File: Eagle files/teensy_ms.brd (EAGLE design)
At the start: 36 x 50 mm, 14 parts, among them IC1 SN65HVD230, IC2 TEENSY_3.0_BASIC-MIN

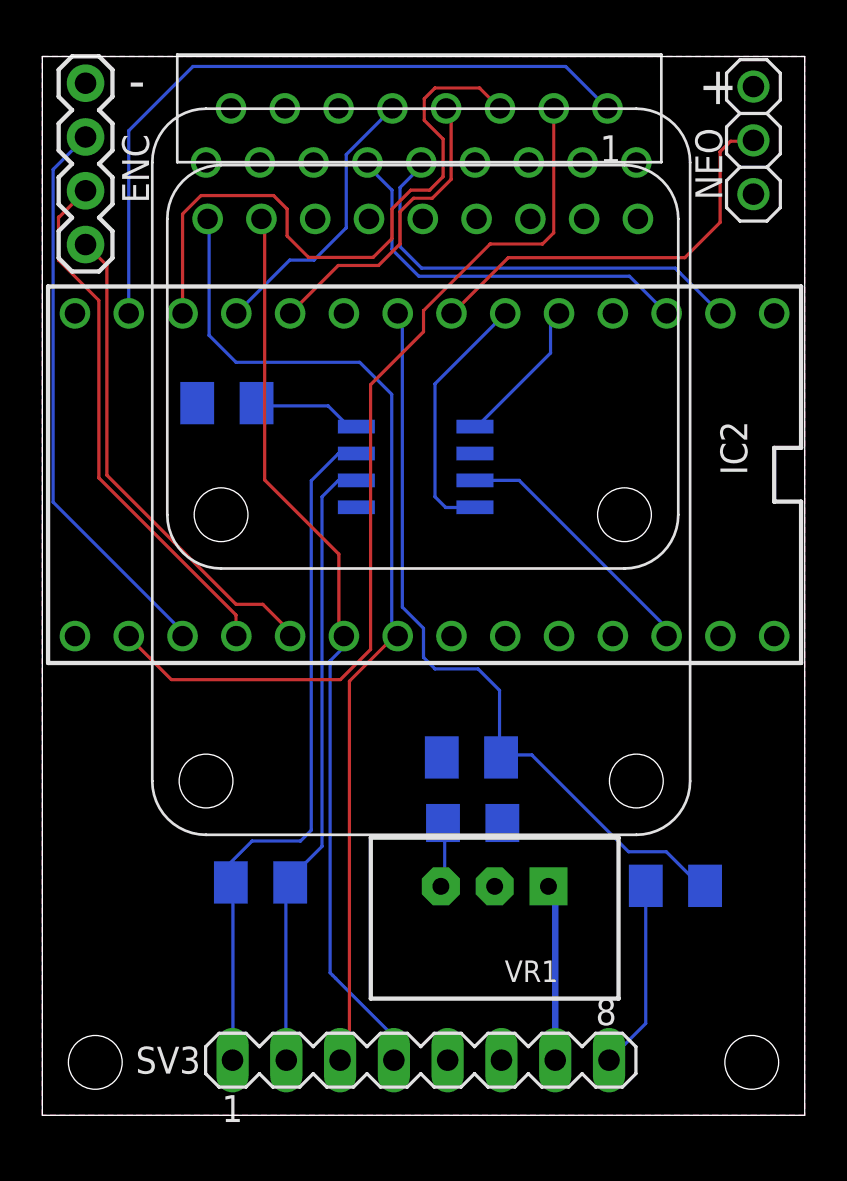
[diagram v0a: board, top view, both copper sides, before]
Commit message: Remove GPS and Accel from PCB
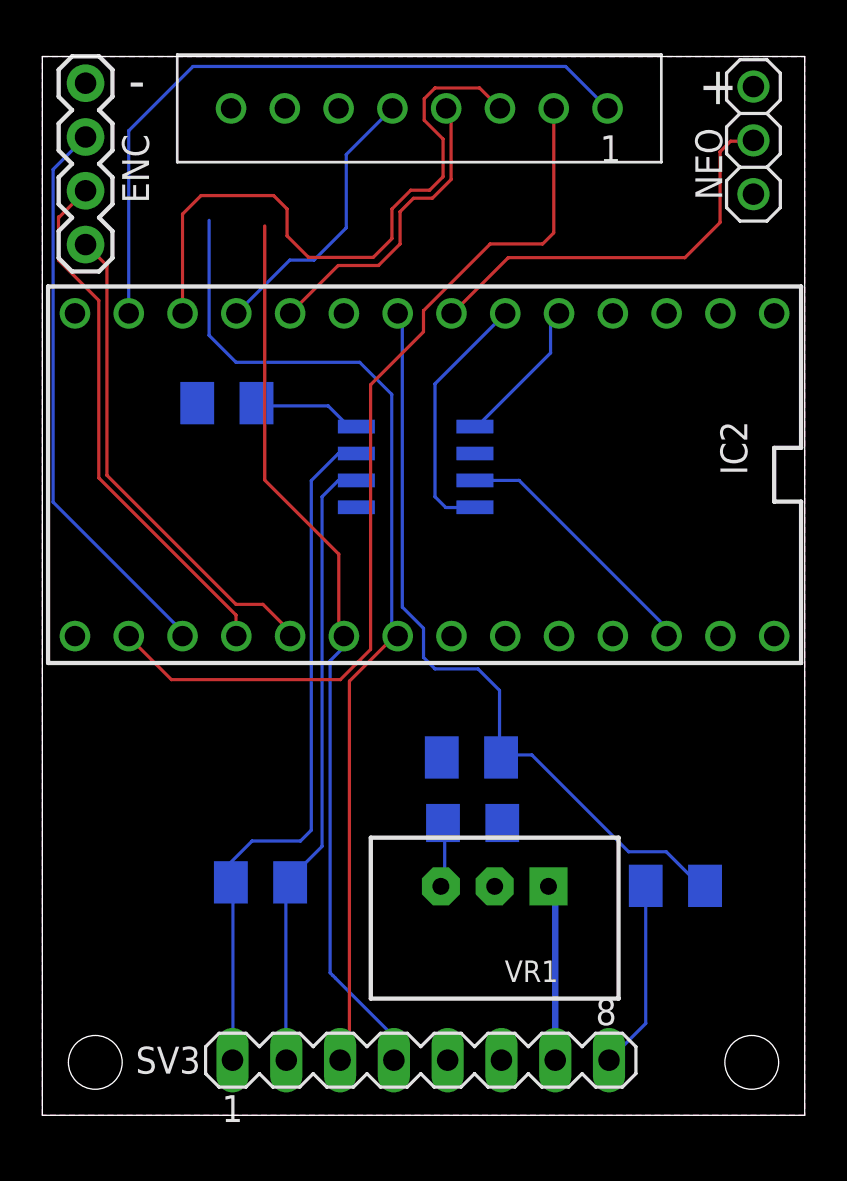
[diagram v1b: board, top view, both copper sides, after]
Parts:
- removed U$3: ACCELEROMETER, custom:ACCELEROMETER
- removed U$5: ULTIMATEGPS, custom:ULTIMATEGPS
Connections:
- removed net N$4: IC2.1, U$5.4
- removed net N$5: IC2.0, U$5.5
- net GND: no longer U$3.7, U$5.3
- net N$14: no longer U$3.1
- net N$16: no longer U$3.2
- net VCC: no longer U$3.9, U$5.2
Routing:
- net N$5: track 20.8 -> 0.00 mm
- net N$4: track 18.8 -> 0.00 mm
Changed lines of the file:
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@@
 <?xml version="1.0" encoding="utf-8"?>
 <!DOCTYPE eagle SYSTEM "eagle.dtd">
-<eagle version="7.1.0">
+<eagle version="9.6.2">
 <drawing>
 <settings>
-<setting alwaysvectorfont="no"/>
+<setting alwaysvectorfont="yes"/>
+<setting keepoldvectorfont="yes"/>
 <setting verticaltext="up"/>
 </settings>
@@
 <param name="dpMaxLengthDifference" value="10mm"/>
 <param name="dpGapFactor" value="2.5"/>
-<param name="checkGrid" value="0"/>
 <param name="checkAngle" value="0"/>
 <param name="checkFont" value="1"/>
 <param name="checkRestrict" value="1"/>
+<param name="checkStop" value="0"/>
+<param name="checkValues" value="0"/>
+<param name="checkNames" value="1"/>
+<param name="checkWireStubs" value="1"/>
+<param name="checkPolygonWidth" value="0"/>
 <param name="useDiameter" value="13"/>
 <param name="maxErrors" value="50"/>
@@
 <attribute name="NAME" x="5.0372" y="43.0758" size="1.27" layer="25" ratio="10" rot="R90"/>
 </element>
-<element name="IC1" library="open-bldc" package="SO8" value="SN65HVD230" x="17.628" y="30.618" rot="MR270"/>
+<element name="IC1" library="open-bldc" package="SO8" value="SN65HVD230" x="17.628" y="30.618" smashed="yes" rot="MR270">
+<attribute name="NAME" x="19.533" y="33.285" size="0.635" layer="26" font="vector" ratio="16" rot="MR0"/>
+<attribute name="VALUE" x="19.533" y="27.2906" size="0.635" layer="28" font="vector" ratio="16" rot="MR0"/>
+</element>
 <element name="NEO" library="adafruit" package="1X03" value="" x="33.58" y="46.04" smashed="yes" rot="R270">
 <attribute name="NAME" x="30.8368" y="46.6242" size="1.27" layer="25" ratio="10" rot="R270"/>
@@
 </element>
 <element name="SV3" library="con-lstb" package="MA08-1" value="" x="17.87" y="2.604" smashed="yes">
+<attribute name="MF" value="" x="17.87" y="2.604" size="1.778" layer="27" display="off"/>
+<attribute name="MPN" value="" x="17.87" y="2.604" size="1.778" layer="27" display="off"/>
+<attribute name="NAME" x="4.408" y="1.969" size="1.27" layer="25" ratio="10"/>
+<attribute name="OC_FARNELL" value="unknown" x="17.87" y="2.604" size="1.778" layer="27" display="off"/>
 <attribute name="OC_NEWARK" value="unknown" x="17.87" y="2.604" size="1.778" layer="27" display="off"/>
-<attribute name="MPN" value="" x="17.87" y="2.604" size="1.778" layer="27" display="off"/>
-<attribute name="MF" value="" x="17.87" y="2.604" size="1.778" layer="27" display="off"/>
-<attribute name="OC_FARNELL" value="unknown" x="17.87" y="2.604" size="1.778" layer="27" display="off"/>
-<attribute name="NAME" x="4.408" y="1.969" size="1.27" layer="25" ratio="10"/>
 <attribute name="VALUE" x="16.6" y="-0.317" size="1.27" layer="27" ratio="10"/>
 </element>
-<element name="IC2" library="Teensy3.0-custom" package="TEESNY_3.0_BASIC-MIN" value="TEENSY_3.0_BASIC-MIN" x="16.78" y="30.25" rot="R270"/>
-<element name="VR1" library="SteelCaveRobotics-Power" package="TSR-1" value="TSR1-2450" x="21.36" y="9.312" rot="R180"/>
-<element name="U$3" library="custom" package="ACCELEROMETER" value="ACCELEROMETER" x="18.6" y="42.332" smashed="yes"/>
+<element name="IC2" library="Teensy3.0-custom" package="TEESNY_3.0_BASIC-MIN" value="TEENSY_3.0_BASIC-MIN" x="16.78" y="30.25" smashed="yes" rot="R270">
+<attribute name="NAME" x="32.02" y="32.79" size="1.27" layer="25" font="vector" rot="R270"/>
+<attribute name="VALUE" x="4.08" y="34.06" size="1.27" layer="27" font="vector" rot="R270"/>
+</element>
+<element name="VR1" library="SteelCaveRobotics-Power" package="TSR-1" value="TSR1-2450" x="21.36" y="9.312" smashed="yes" rot="R180">
+<attribute name="NAME" x="24.36" y="7.312" size="1.016" layer="25" rot="R180"/>
+<attribute name="VALUE" x="24.36" y="9.312" size="1.016" layer="27" rot="R180"/>
+</element>
 <element name="U$4" library="custom" package="OLED-1.3-BARE" value="OLED-1.3MINIMAL" x="17.8" y="47.55" smashed="yes" rot="R180"/>
-<element name="U$5" library="custom" package="ULTIMATEGPS" value="ULTIMATEGPS" x="17.89" y="44.996" smashed="yes">
-<attribute name="VALUE" x="6.46" y="42.456" size="1.27" layer="27"/>
-</element>
 </elements>
 <signals>
@@
 </signal>
 <signal name="GND">
-<contactref element="U$5" pad="3"/>
-<contactref element="U$3" pad="7"/>
 <contactref element="U$4" pad="8"/>
 <contactref element="IC1" pad="2"/>
@@
 <vertex x="0" y="0"/>
 </polygon>
+<wire x1="34.56" y1="37.87" x2="33.58" y2="43.5" width="0" layer="19" extent="1-1"/>
+<wire x1="20.428" y1="31.253" x2="34.56" y2="37.87" width="0" layer="19" extent="16-16"/>
+<wire x1="7.314" y1="33.632" x2="20.428" y2="31.253" width="0" layer="19" extent="16-16"/>
+<wire x1="8.91" y1="47.55" x2="7.314" y2="33.632" width="0" layer="19" extent="16-16"/>
+<wire x1="2.04" y1="48.74" x2="8.91" y2="47.55" width="0" layer="19" extent="1-1"/>
+<wire x1="18.862" y1="16.9" x2="20.428" y2="31.253" width="0" layer="19" extent="16-16"/>
+<wire x1="21.72" y1="13.804" x2="18.862" y2="16.9" width="0" layer="19" extent="16-16"/>
+<wire x1="21.36" y1="10.812" x2="21.72" y2="13.804" width="0" layer="19" extent="16-16"/>
+<wire x1="21.68" y1="2.604" x2="21.36" y2="10.812" width="0" layer="19" extent="1-1"/>
 </signal>
 <signal name="VCC">
@@
 <contactref element="SV3" pad="5"/>
 <contactref element="C1" pad="1"/>
-<contactref element="U$3" pad="9"/>
-<contactref element="U$5" pad="2"/>
 <contactref element="U$4" pad="7"/>
 <polygon width="0.4064" layer="1">
@@
 <wire x1="19" y1="14.5" x2="18.92" y2="13.804" width="0.1524" layer="16"/>
 <wire x1="19" y1="11" x2="18.82" y2="10.812" width="0.1524" layer="16"/>
-</signal>
-<signal name="N$4">
-<contactref element="IC2" pad="1"/>
-<contactref element="U$5" pad="4"/>
-<wire x1="29.48" y1="37.87" x2="27.726" y2="39.624" width="0.1524" layer="16"/>
-<wire x1="27.726" y1="39.624" x2="17.78" y2="39.624" width="0.1524" layer="16"/>
-<wire x1="17.78" y1="39.624" x2="16.51" y2="40.894" width="0.1524" layer="16"/>
-<wire x1="16.51" y1="40.894" x2="16.51" y2="43.688" width="0.1524" layer="16"/>
-<wire x1="16.51" y1="43.688" x2="15.35" y2="44.848" width="0.1524" layer="16"/>
-<wire x1="15.35" y1="44.848" x2="15.35" y2="44.996" width="0.1524" layer="16"/>
-</signal>
-<signal name="N$5">
-<contactref element="IC2" pad="0"/>
-<contactref element="U$5" pad="5"/>
-<wire x1="32.02" y1="37.87" x2="30.119" y2="39.771" width="0.1524" layer="16"/>
-<wire x1="30.119" y1="39.771" x2="30.012" y2="39.878" width="0.1524" layer="16"/>
-<wire x1="16.891" y1="41.021" x2="16.891" y2="43.815" width="0.1524" layer="16"/>
-<wire x1="16.891" y1="43.815" x2="17.89" y2="44.814" width="0.1524" layer="16"/>
-<wire x1="17.89" y1="44.814" x2="17.89" y2="44.996" width="0.1524" layer="16"/>
-<wire x1="16.891" y1="41.021" x2="17.907" y2="40.005" width="0.1524" layer="16"/>
-<wire x1="17.907" y1="40.005" x2="29.885" y2="40.005" width="0.1524" layer="16"/>
-<wire x1="29.885" y1="40.005" x2="30.012" y2="39.878" width="0.1524" layer="16"/>
+<wire x1="11.45" y1="47.55" x2="33.58" y2="48.58" width="0" layer="19" extent="1-1"/>
+<wire x1="34.56" y1="22.63" x2="33.58" y2="48.58" width="0" layer="19" extent="1-1"/>
+<wire x1="18.92" y1="13.804" x2="34.56" y2="22.63" width="0" layer="19" extent="16-16"/>
+<wire x1="19.14" y1="2.604" x2="18.82" y2="10.812" width="0" layer="19" extent="1-1"/>
 </signal>
 <signal name="N$8">
@@
 <signal name="N$16">
 <contactref element="IC2" pad="18/A4"/>
-<contactref element="U$3" pad="2"/>
 <contactref element="SV3" pad="4"/>
 <wire x1="10.5" y1="30" x2="10.5" y2="42" width="0.1524" layer="1"/>
 <wire x1="14" y1="26.5" x2="10.5" y2="30" width="0.1524" layer="1"/>
 <wire x1="14" y1="23" x2="14" y2="26.5" width="0.1524" layer="1"/>
-<wire x1="10.5" y1="42" x2="10.345" y2="42.332" width="0.1524" layer="1"/>
 <wire x1="14" y1="23" x2="14.24" y2="22.63" width="0.1524" layer="1"/>
 <wire x1="16.6" y1="2.604" x2="16.51" y2="2.694" width="0.1524" layer="16"/>
@@
 <signal name="N$14">
 <contactref element="IC2" pad="19/A5"/>
-<contactref element="U$3" pad="1"/>
 <contactref element="SV3" pad="3"/>
 <wire x1="14.5" y1="20.5" x2="16.5" y2="22.5" width="0.1524" layer="1"/>
@@
 <wire x1="9.144" y1="35.56" x2="7.874" y2="36.83" width="0.1524" layer="16"/>
 <wire x1="7.874" y1="36.83" x2="7.874" y2="42.263" width="0.1524" layer="16"/>
-<wire x1="7.874" y1="42.263" x2="7.805" y2="42.332" width="0.1524" layer="16"/>
 <wire x1="16.5" y1="34.046" x2="14.986" y2="35.56" width="0.1524" layer="16"/>
 </signal>
 </signals>
+<mfgpreviewcolors>
+<mfgpreviewcolor name="soldermaskcolor" color="0xC8008000"/>
+<mfgpreviewcolor name="silkscreencolor" color="0xFFFEFEFE"/>
+<mfgpreviewcolor name="backgroundcolor" color="0xFF282828"/>
+<mfgpreviewcolor name="coppercolor" color="0xFFFFBF00"/>
+<mfgpreviewcolor name="substratecolor" color="0xFF786E46"/>
+</mfgpreviewcolors>
 <errors>
 </errors>
